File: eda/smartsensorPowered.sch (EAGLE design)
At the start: 36 parts, among them Q1 IRFML8244, Q2 IRFML8244, Q3 IRFML8244, Q4 IRFML8244, U1 ISL83491SOIC, U2 ATTINY1634

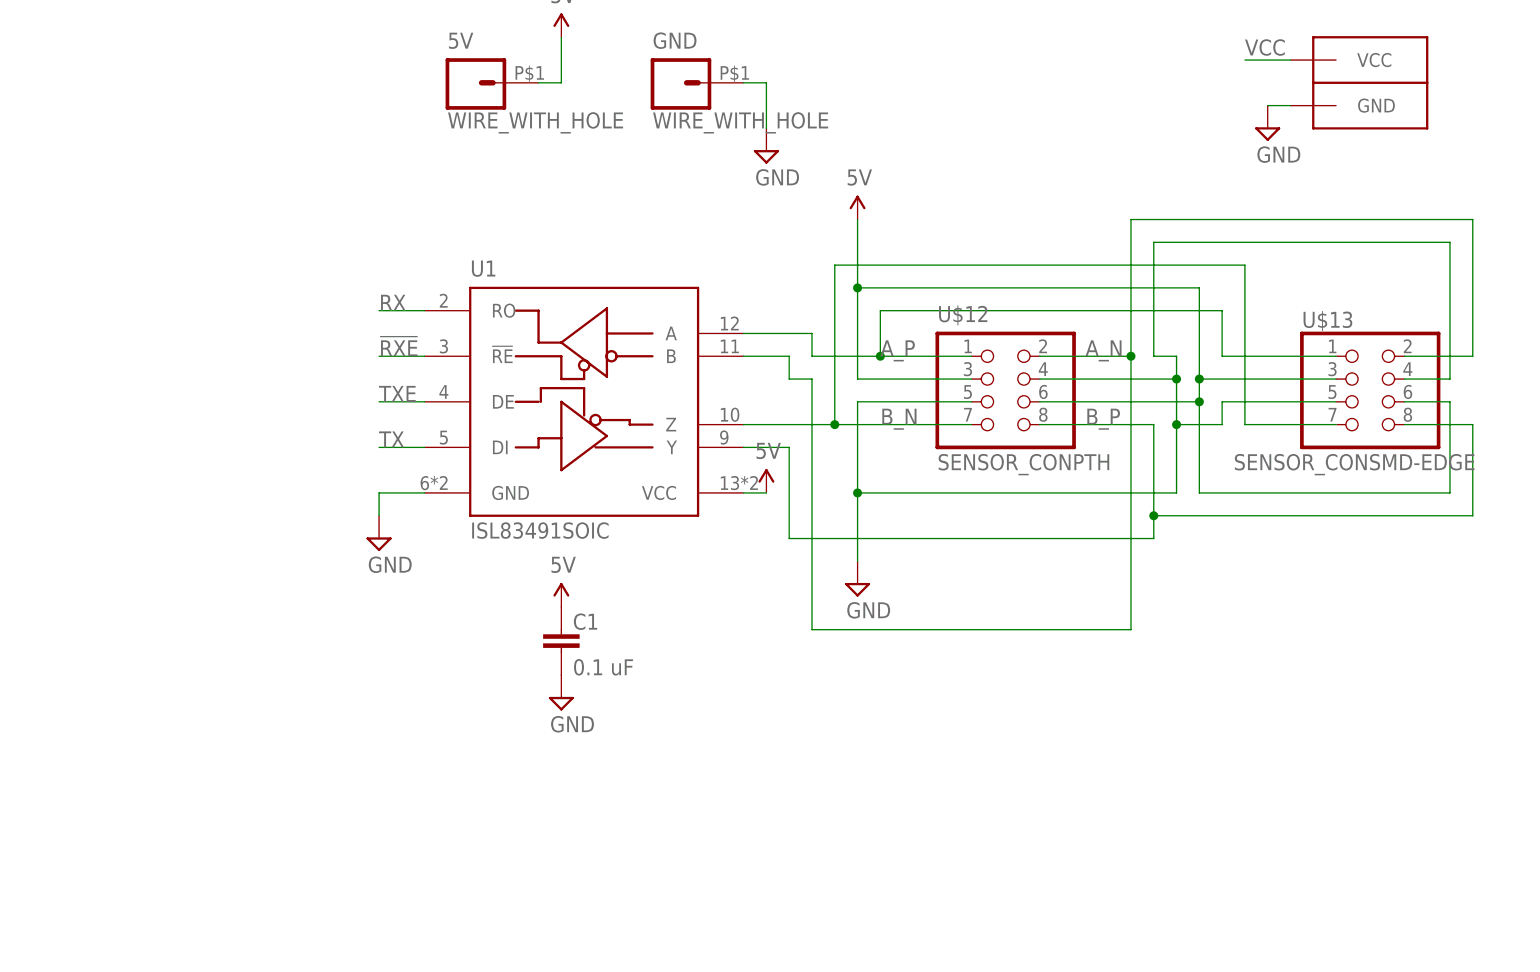
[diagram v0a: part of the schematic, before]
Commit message: Replaced 2x4 connectors with 2x5's.
On smartsensor, smartsensorPowered, smartsensor_powered_jig, and team_flag.
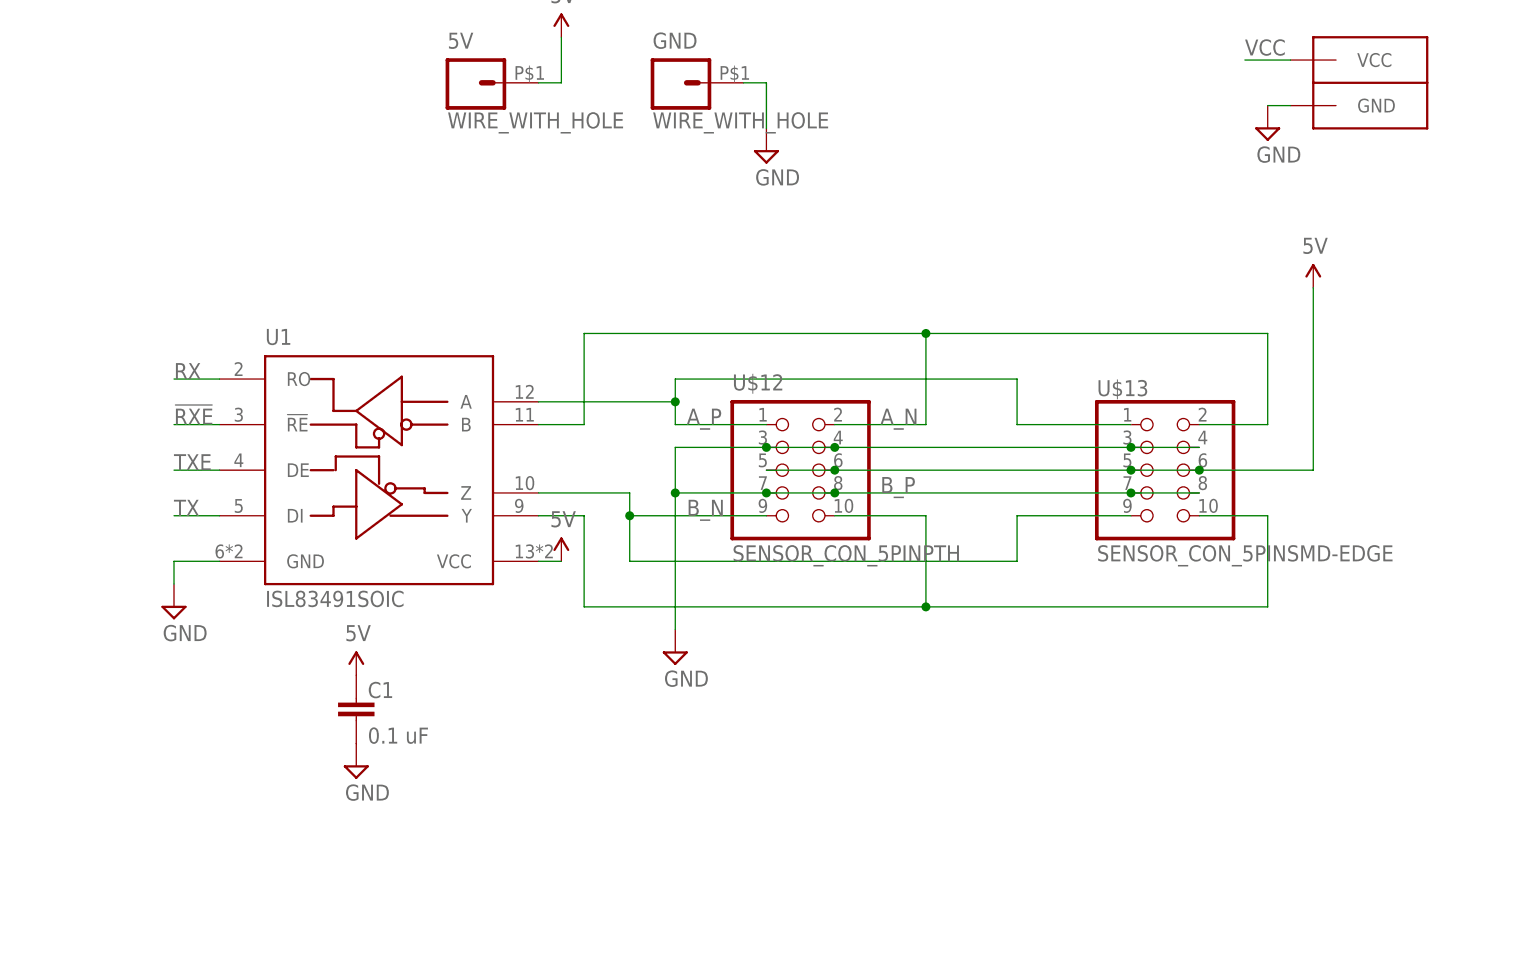
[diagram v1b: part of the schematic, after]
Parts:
- U$12: value SENSOR_CONPTH -> SENSOR_CON_5PINPTH; device pie:SENSOR_CONPTH -> pie:SENSOR_CON_5PINPTH
- U$13: value SENSOR_CONSMD-EDGE -> SENSOR_CON_5PINSMD-EDGE; device pie:SENSOR_CONSMD-EDGE -> pie:SENSOR_CON_5PINSMD-EDGE
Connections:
- net 5V: now also U$12.5, U$13.5; no longer U$12.3, U$13.3
- net B_N: now also U$12.9, U$13.9; no longer U$12.7, U$13.7
- net B_P: now also U$12.10, U$13.10; no longer U$12.8, U$13.8
- net GND: now also U$12.3, U$12.7, U$12.8, U$13.3, U$13.7, U$13.8; no longer U$12.5, U$13.5
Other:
- moved on the sheet: C1, U1
